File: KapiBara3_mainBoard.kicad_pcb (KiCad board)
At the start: 4 copper layers, 129.5 x 129.5 mm, 44 parts, among them J1 Conn_02x20_Top_Bottom, J2 Conn_02x20_Top_Bottom, J3 Conn_02x20_Top_Bottom, J4 Conn_02x20_Top_Bottom, J5 Conn_02x20_Top_Bottom, J6 Conn_01x02, J7 Conn_01x08, J8 Conn_01x02, J9 Conn_01x02, Q1 Q_PMOS_GDS, Q2 2N7002, Q3 Q_PMOS_GDS, U1 SL2.1A, U2 AP63300WU-7, U3 ADS1115IDGS, Y1 12Mhz

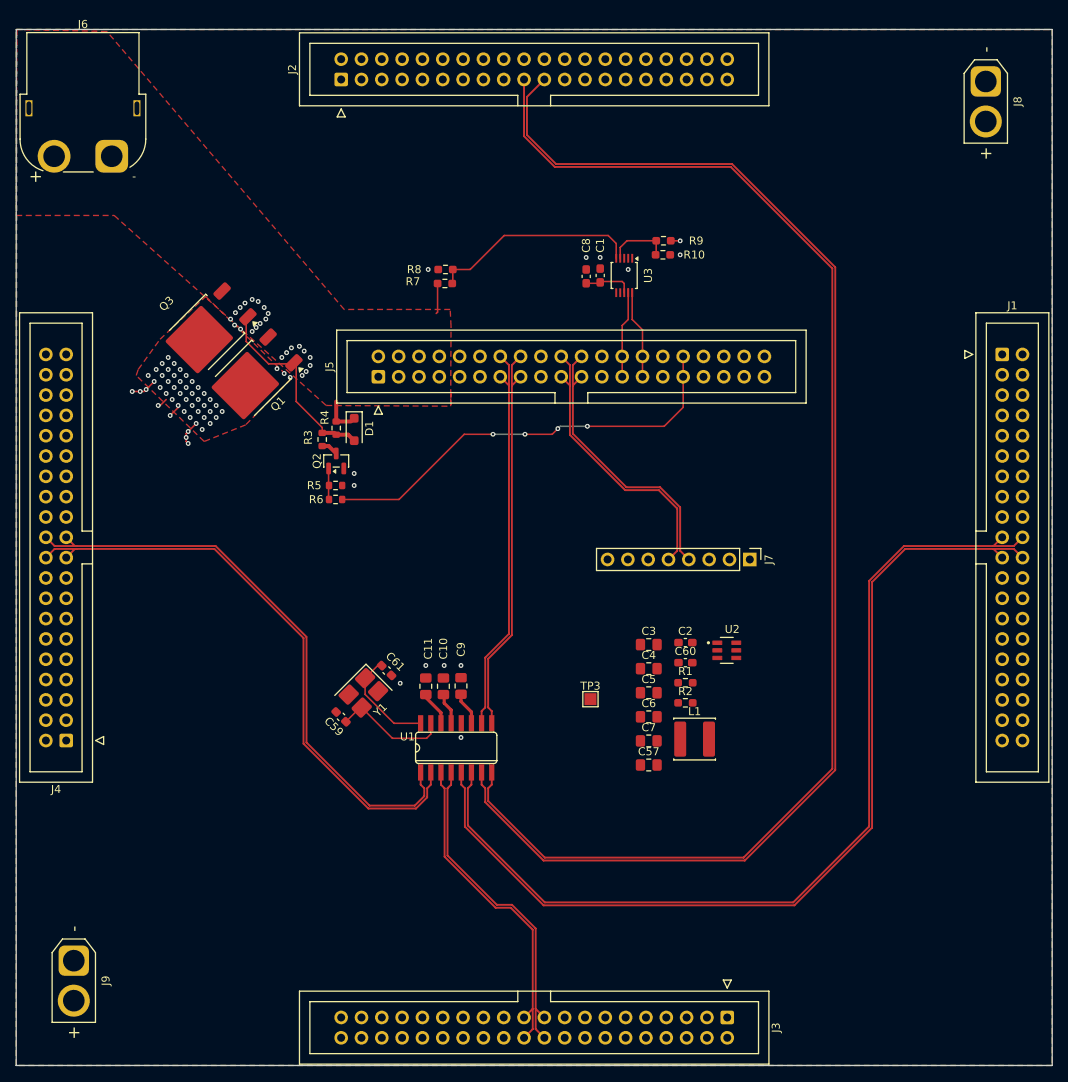
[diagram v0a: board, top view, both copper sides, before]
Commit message: Added mouting holes
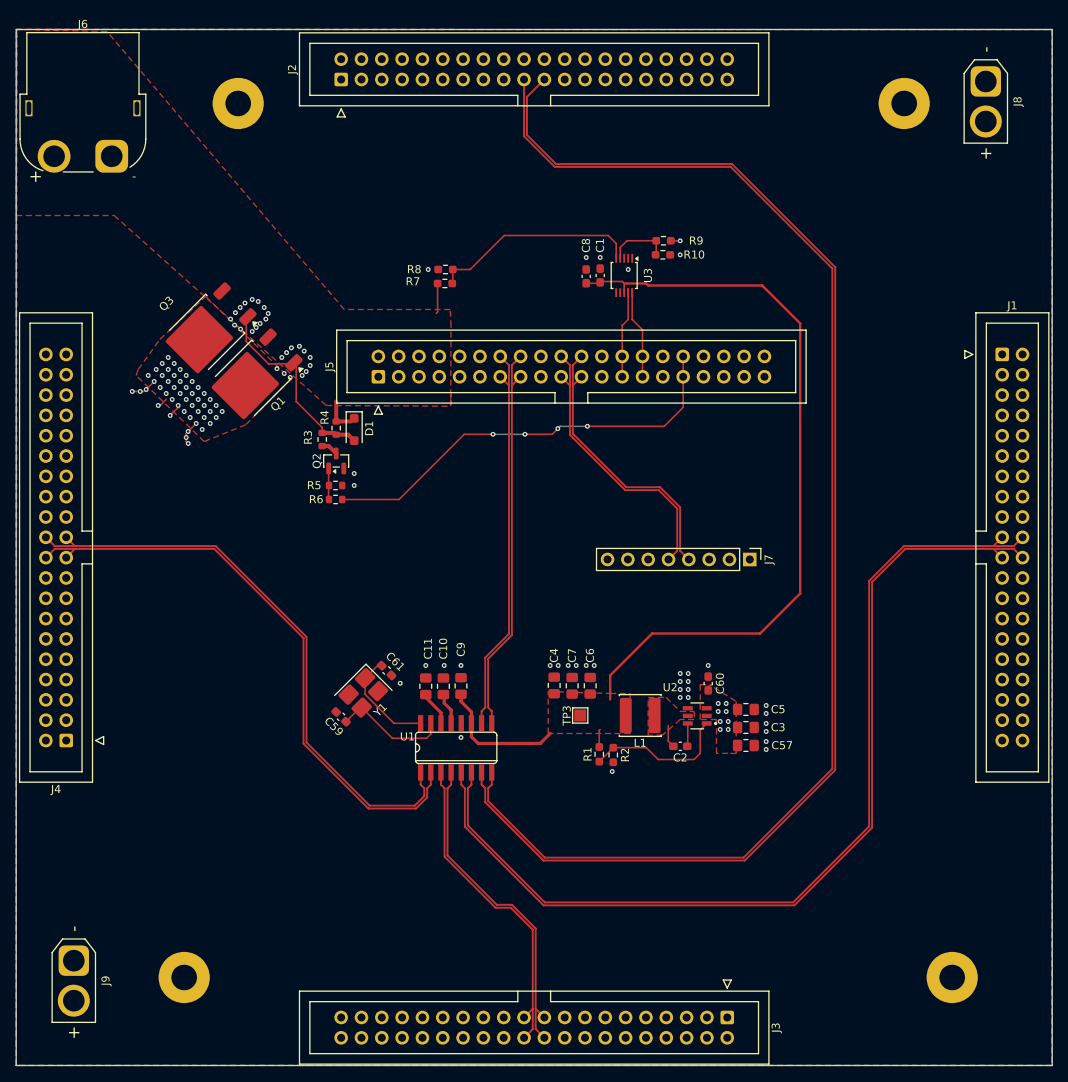
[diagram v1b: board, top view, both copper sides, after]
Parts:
- added ?: , , F.Cu at (27.8, 9.00)
- added REF**: MountingHole_3.2mm_M3_Pad, MountingHole:MountingHole_3.2mm_M3_Pad, F.Cu at (117.0, 118.5)
- added REF**: MountingHole_3.2mm_M3_Pad, MountingHole:MountingHole_3.2mm_M3_Pad, F.Cu at (111.0, 9.25)
- added REF**: MountingHole_3.2mm_M3_Pad, MountingHole:MountingHole_3.2mm_M3_Pad, F.Cu at (21.0, 118.5)
- moved C3 16.0 mm to (91.2, 87.2)
- moved R1 14.0 mm to (72.9, 90.6), turned to 90 degrees
- moved C2 13.0 mm to (83.0, 89.6), turned to 180 degrees
- moved C57 12.4 mm to (91.2, 89.5)
- moved C5 12.3 mm to (91.2, 85.0)
- moved C4 12.0 mm to (67.2, 82.0), turned to 90 degrees
- moved C7 11.8 mm to (69.5, 82.0), turned to 90 degrees
- moved R2 11.1 mm to (74.6, 90.7), turned to 90 degrees
- moved U2 8.98 mm to (85.1, 85.8), turned to 180 degrees
- moved C6 8.29 mm to (71.8, 82.0), turned to 90 degrees
- moved L1 7.41 mm to (78.0, 85.8), turned to 180 degrees
- moved C60 3.86 mm to (86.5, 81.8), turned to 90 degrees
- moved TP3 2.41 mm to (70.5, 85.8), turned to 90 degrees
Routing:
- net +5V: track 10.3 -> 113.7 mm
- net Net-(U2-FB): track 0.00 -> 18.3 mm
- net Net-(U2-BST): track 0.00 -> 2.88 mm
- net Net-(U2-SW): track 0.00 -> 2.87 mm
- net VCC: vias 49 -> 57
- net GND: vias 38 -> 60
- added copper zone on F.Cu, net +5V
- added copper zone on F.Cu, net Net-(U2-SW)

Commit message: I need to think what else to add
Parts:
- added C12: 22u, Capacitor_SMD:C_0805_2012Metric_Pad1.18x1.45mm_HandSolder, F.Cu at (91.2, 91.8)
- added C13: 22u, Capacitor_SMD:C_0805_2012Metric_Pad1.18x1.45mm_HandSolder, F.Cu at (91.2, 94.0)
- added C14: 22u, Capacitor_SMD:C_0805_2012Metric_Pad1.18x1.45mm_HandSolder, F.Cu at (86.5, 94.2)
- added D10: TVS, Diode_SMD:D_SOD-323, F.Cu at (68.5, 14.0)
- added D11: TVS, Diode_SMD:D_SOD-323, F.Cu at (64.2, 18.0)
- added D12: TVS, Diode_SMD:D_SOD-323, F.Cu at (80.0, 63.0)
- added D13: TVS, Diode_SMD:D_SOD-323, F.Cu at (85.5, 63.0)
- added D14: TVS, Diode_SMD:D_SOD-323, F.Cu at (59.2, 48.8)
- added D15: TVS, Diode_SMD:D_SOD-323, F.Cu at (64.3, 48.5)
- added D2: LED, LED_SMD:LED_0805_2012Metric_Pad1.15x1.40mm_HandSolder, F.Cu at (5.48, 24.8)
- added D3: LED, LED_SMD:LED_0805_2012Metric_Pad1.15x1.40mm_HandSolder, F.Cu at (5.47, 28.2)
- added D4: TVS, Diode_SMD:D_SOD-323, F.Cu at (19.8, 61.8)
- added D5: TVS, Diode_SMD:D_SOD-323, F.Cu at (19.8, 67.7)
- added D6: TVS, Diode_SMD:D_SOD-323, F.Cu at (61.5, 116.8)
- added D7: TVS, Diode_SMD:D_SOD-323, F.Cu at (68.0, 116.8)
- added D8: TVS, Diode_SMD:D_SOD-323, F.Cu at (116.0, 67.2)
- added D9: TVS, Diode_SMD:D_SOD-323, F.Cu at (116.0, 62.0)
- added R11: 1k, Resistor_SMD:R_0603_1608Metric, F.Cu at (9.57, 24.8)
- added R12: 1k, Resistor_SMD:R_0603_1608Metric, F.Cu at (9.57, 28.2)
- added TP1: TestPoint, TestPoint:TestPoint_Pad_D1.5mm, F.Cu at (15.8, 61.5)
- added TP10: TestPoint, TestPoint:TestPoint_Pad_D1.5mm, F.Cu at (71.0, 57.5)
- added TP11: TestPoint, TestPoint:TestPoint_Pad_D1.5mm, F.Cu at (79.0, 54.0)
- added TP12: TestPoint, TestPoint:TestPoint_Pad_1.5x1.5mm, F.Cu at (40.2, 24.5)
- added TP13: TestPoint, TestPoint:TestPoint_Pad_1.5x1.5mm, F.Cu at (21.5, 20.8)
- added TP14: TestPoint, TestPoint:TestPoint_Pad_D3.0mm, F.Cu at (32.8, 17.8)
- added TP15: TestPoint, TestPoint:TestPoint_Pad_D3.0mm, F.Cu at (6.75, 107.8)
- added TP16: TestPoint, TestPoint:TestPoint_Pad_D3.0mm, F.Cu at (115.8, 107.5)
- added TP17: TestPoint, TestPoint:TestPoint_Pad_D3.0mm, F.Cu at (121.5, 21.0)
- added TP18: TestPoint, TestPoint:TestPoint_Pad_D1.5mm, F.Cu at (74.8, 48.8)
- added TP19: TestPoint, TestPoint:TestPoint_Pad_D1.5mm, F.Cu at (79.5, 48.8)
- added TP2: TestPoint, TestPoint:TestPoint_Pad_D1.5mm, F.Cu at (15.8, 67.0)
- added TP4: TestPoint, TestPoint:TestPoint_Pad_D1.5mm, F.Cu at (68.8, 113.5)
- added TP5: TestPoint, TestPoint:TestPoint_Pad_D1.5mm, F.Cu at (61.0, 114.2)
- added TP6: TestPoint, TestPoint:TestPoint_Pad_D1.5mm, F.Cu at (113.2, 61.5)
- added TP7: TestPoint, TestPoint:TestPoint_Pad_D1.5mm, F.Cu at (113.2, 68.2)
- added TP8: TestPoint, TestPoint:TestPoint_Pad_D1.5mm, F.Cu at (90.8, 23.0)
- added TP9: TestPoint, TestPoint:TestPoint_Pad_D1.5mm, F.Cu at (96.0, 19.0)
- moved REF** 0.25 mm to (111.0, 9.00)
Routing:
- net D_1+: track 35.8 -> 42.5 mm
- net D2+: track 41.0 -> 47.4 mm
- net SCL: track 11.5 -> 17.4 mm
- net SDA: track 11.3 -> 17.1 mm
- net D2-: track 41.0 -> 46.6 mm
- net D4+: track 169.3 -> 174.4 mm
- net D4-: track 171.4 -> 176.4 mm
- net D1-: track 74.4 -> 79.2 mm
- net D_1-: track 35.8 -> 40.6 mm
- net D3-: track 119.2 -> 123.8 mm
- net D3+: track 118.6 -> 123.2 mm
- net D1+: track 75.0 -> 78.8 mm
- net VCC: track 10.5 -> 13.9 mm, vias 57 -> 67
- net Net-(D3-A): track 0.00 -> 2.25 mm
- net Net-(D2-A): track 0.00 -> 2.25 mm
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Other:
- board text added: "PWR_IN"
- board text added: "PWR_ON"

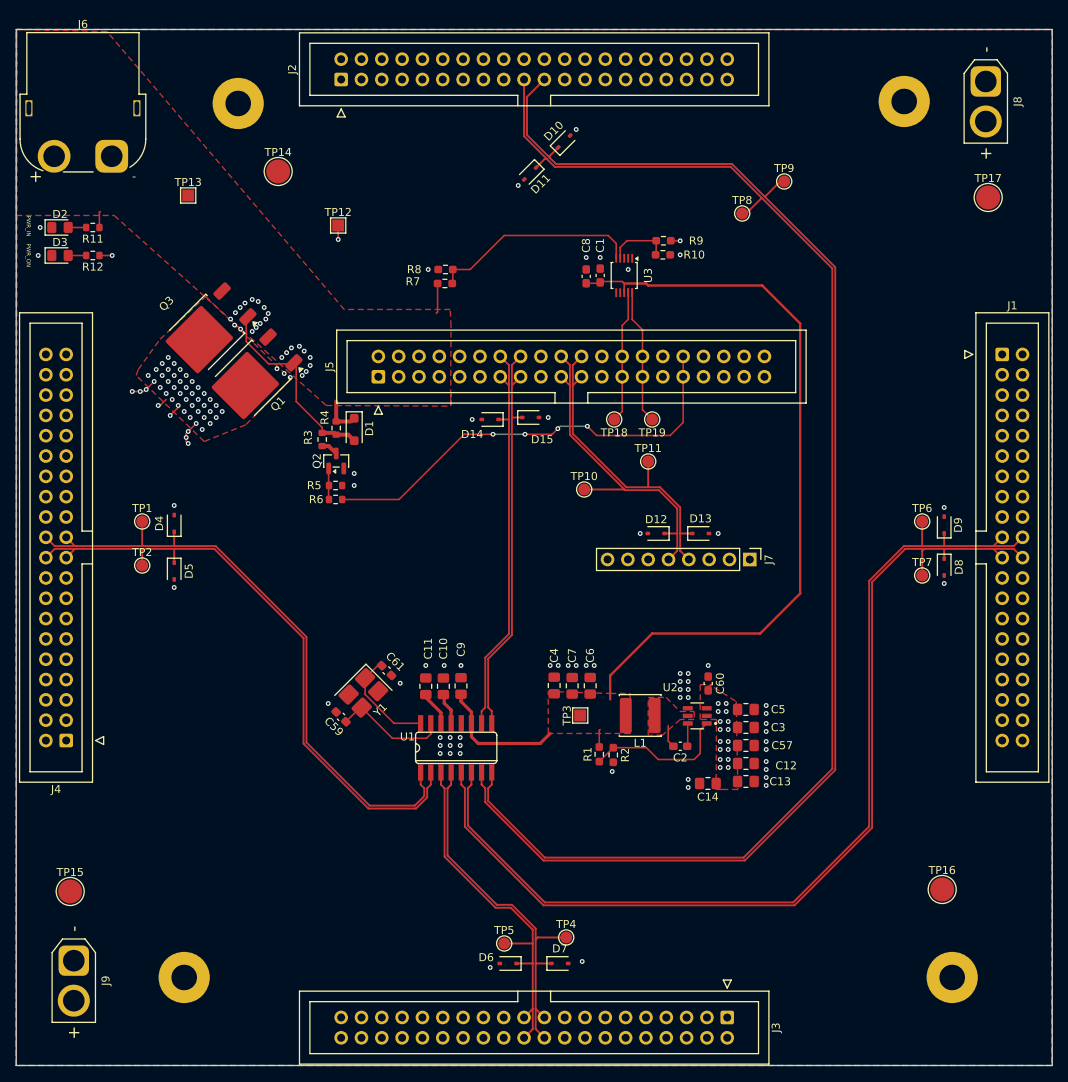
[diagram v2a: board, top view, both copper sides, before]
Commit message: Added some offsets to board outlines
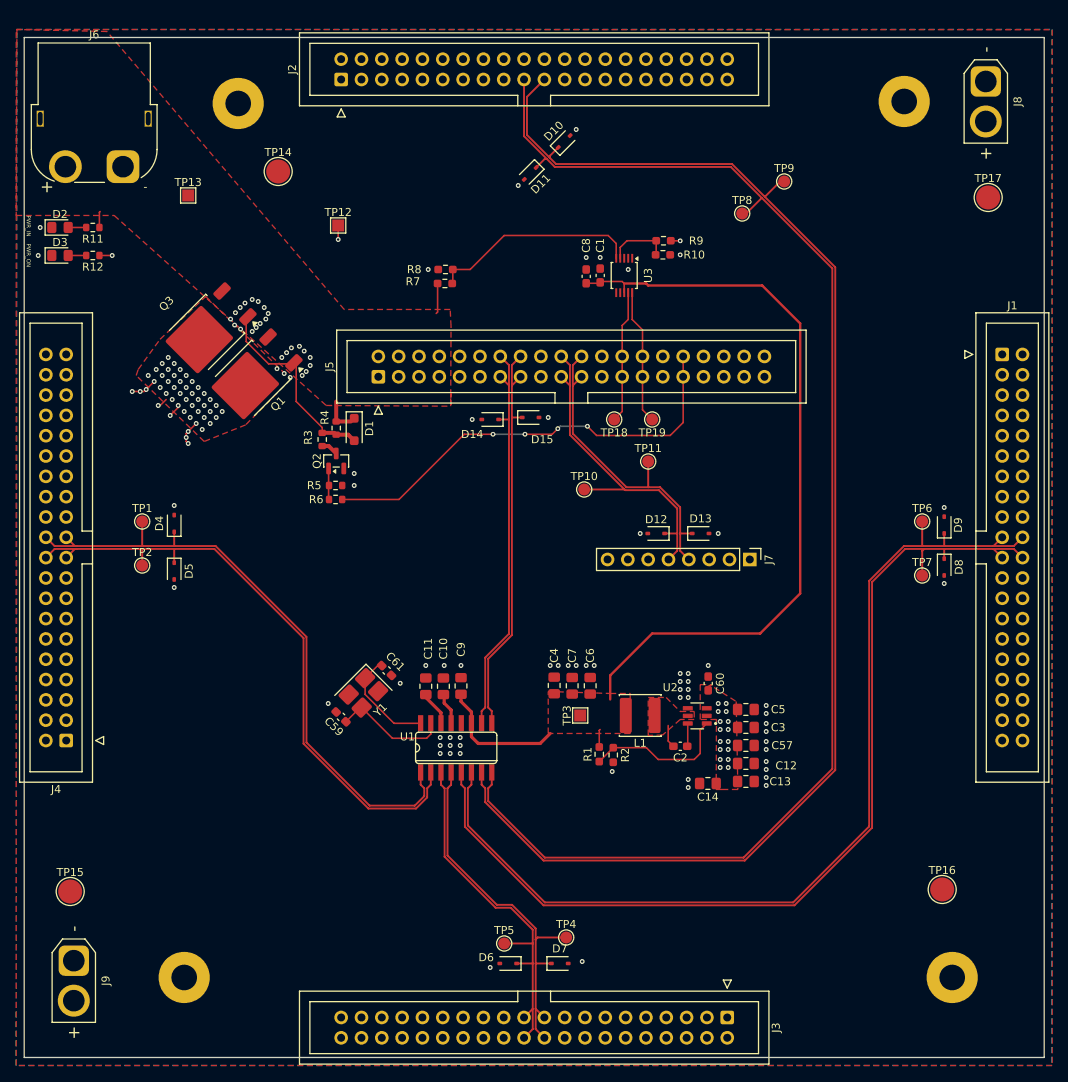
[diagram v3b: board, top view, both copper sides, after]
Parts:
- moved J6 1.92 mm to (13.3, 17.1)
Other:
- board size 129.5 x 129.5 mm -> 127.5 x 127.5 mm
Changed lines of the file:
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@@
 		(locked yes)
 		(layer "F.Cu")
-		(at 11.94 15.85)
+		(at 13.35 17.15)
 		(descr "Connector XT60 Horizontal PCB Female, https://www.tme.eu/Document/1191bc2fa3aee3c446e5a895fd8f7983/XT60PW-F.pdf")
 		(tags "RC Connector XT60")
@@
 	)
 	(gr_rect
-		(start 0 0)
-		(end 129.5 129.5)
+		(start 1 1)
+		(end 128.5 128.5)
 		(stroke
 			(width 0.05)

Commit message: I have shrinken down the board
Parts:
- removed the REF** at (111.0, 9.00)
- added ?: , , F.Cu at (93.5, 31.0)
- added J10: Conn_01x02, Connector_AMASS:AMASS_XT30U-F_1x02_P5.0mm_Vertical, F.Cu at (90.2, 56.8)
- added J11: Conn_01x02, Connector_AMASS:AMASS_XT30U-F_1x02_P5.0mm_Vertical, F.Cu at (35.8, 110.8)
- added J12: Conn_01x02, Connector_AMASS:AMASS_XT30U-F_1x02_P5.0mm_Vertical, F.Cu at (24.8, 93.5)
- added J13: Conn_01x02, Connector_AMASS:AMASS_XT30U-F_1x02_P5.0mm_Vertical, F.Cu at (111.0, 44.9)
- added J14: Conn_01x02, Connector_AMASS:AMASS_XT30U-F_1x02_P5.0mm_Vertical, F.Cu at (58.2, 18.2)
- added REF**: MountingHole_3.2mm_M3_Pad, MountingHole:MountingHole_3.2mm_M3_Pad, F.Cu at (22.8, 79.8)
- added REF**: MountingHole_3.2mm_M3_Pad, MountingHole:MountingHole_3.2mm_M3_Pad, F.Cu at (51.8, 65.5)
- added REF**: MountingHole_3.2mm_M3_DIN965_Pad, MountingHole:MountingHole_3.2mm_M3_DIN965_Pad, F.Cu at (45.2, 30.5)
- J1, J2, J3, J4: value Conn_02x20_Top_Bottom -> Conn_01x04_MountingPin; footprint Connector_IDC:IDC-Header_2x20_P2.54mm_Vertical -> Connector_FFC-FPC:Amphenol_F32Q-1A7x1-11004_1x04-1MP_P0.5mm_Horizontal
- J6: footprint Connector_AMASS:AMASS_XT60PW-F_1x02_P7.20mm_Horizontal -> Connector_AMASS:AMASS_XT60-M_1x02_P7.20mm_Vertical
- moved J2 106.5 mm to (53.8, 111.9), turned to 0 degrees
- moved J4 99.1 mm to (75.0, 17.5)
- moved J3 90.7 mm to (17.5, 67.5)
- moved TP12 77.0 mm to (39.5, 101.5)
- moved D3 41.8 mm to (46.2, 19.0), turned to -90 degrees
- moved D2 37.2 mm to (42.2, 19.1), turned to -90 degrees
- moved R12 37.0 mm to (46.2, 23.1), turned to 90 degrees
- moved R11 32.7 mm to (42.2, 23.1), turned to 90 degrees
- moved TP15 27.1 mm to (32.0, 98.0)
- moved J1 26.9 mm to (111.9, 65.0), turned to 90 degrees
- moved J9 25.5 mm to (18.5, 93.5)
- moved TP14 24.7 mm to (56.2, 25.5), turned to 180 degrees
- moved D10 20.7 mm to (88.2, 20.2), turned to 90 degrees
- moved TP8 18.8 mm to (72.0, 23.0)
- moved TP16 17.0 mm to (111.5, 91.0)
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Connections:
- J1 pad 1: VCC -> GND
- J1 pad 2: VCC -> D3-
- J1 pad 3: VCC -> D3+
- J1 pad 4: VCC -> GND
- J2 pad 1: VCC -> GND
- J2 pad 2: VCC -> D2-
- J2 pad 3: VCC -> D2+
- J2 pad 4: VCC -> GND
- J3 pad 1: VCC -> GND
- J3 pad 2: VCC -> D1-
- J3 pad 3: VCC -> D1+
- J3 pad 4: VCC -> GND
- J4 pad 1: VCC -> GND
- J4 pad 2: VCC -> D4-
- J4 pad 3: VCC -> D4+
- J4 pad 4: VCC -> GND
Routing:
- net D2+: track 47.4 -> 20.6 mm
- net D2-: track 46.6 -> 20.5 mm
- net D4-: track 176.4 -> 156.2 mm
- net D3+: track 123.2 -> 103.6 mm
- net D3-: track 123.8 -> 104.7 mm
- net D4+: track 174.4 -> 156.2 mm
- net D1-: track 79.2 -> 61.7 mm
- net D1+: track 78.8 -> 61.5 mm
- net VDD: track 10.8 -> 23.9 mm
- net Net-(U3-AIN1): track 26.2 -> 14.1 mm
- net Net-(D1-A): track 25.0 -> 28.6 mm
- net SCL: track 17.4 -> 15.1 mm
- net SDA: track 17.1 -> 14.8 mm
- net +5V: track 113.7 -> 112.2 mm
- net GND: vias 89 -> 211
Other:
- board size 127.5 x 127.5 mm -> 100 x 100 mm
- board text added: "Carrier board mount"
- board text added: "Made by Patryk Peroński 2026"

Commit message: Final design
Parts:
- added G***: LOGO, LOGO, F.Cu at (40.6, 68.4)
- added G***: LOGO, LOGO, F.Cu at (70.0, 98.0)
- added G***: LOGO, LOGO, B.Cu at (61.7, 31.8)
- added G***: LOGO, LOGO, B.Cu at (94.1, 109.9)
- J11, J13, J14, J9: moved to B.Cu
- moved J8 1.40 mm to (109.5, 20.1)
- turned TP17 to 90 degrees
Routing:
- net VDD: track 23.9 -> 26.3 mm
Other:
- board text added: "<- Main power <- goes there"
- board text added: "And here is USB 2 ->"
- board text added: "For extra power use these ->"
- board text added: "Here is USB 3 ->"
- board text added: "KapiBara Qubic Splice Board v1.0"
- board text added: "Made by Patryk Peroński 2026, proudly presents:"
- board text added: "USB 4 right there ->"
- board text added: "USB'y everything!!"
- board text added: "Works with voltages from 5V to 32V!!"
- board text added: "↓USB 1 down here↓"
- board text removed: "Made by Patryk Peroński 2026"
